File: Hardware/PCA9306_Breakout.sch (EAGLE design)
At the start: 15 parts

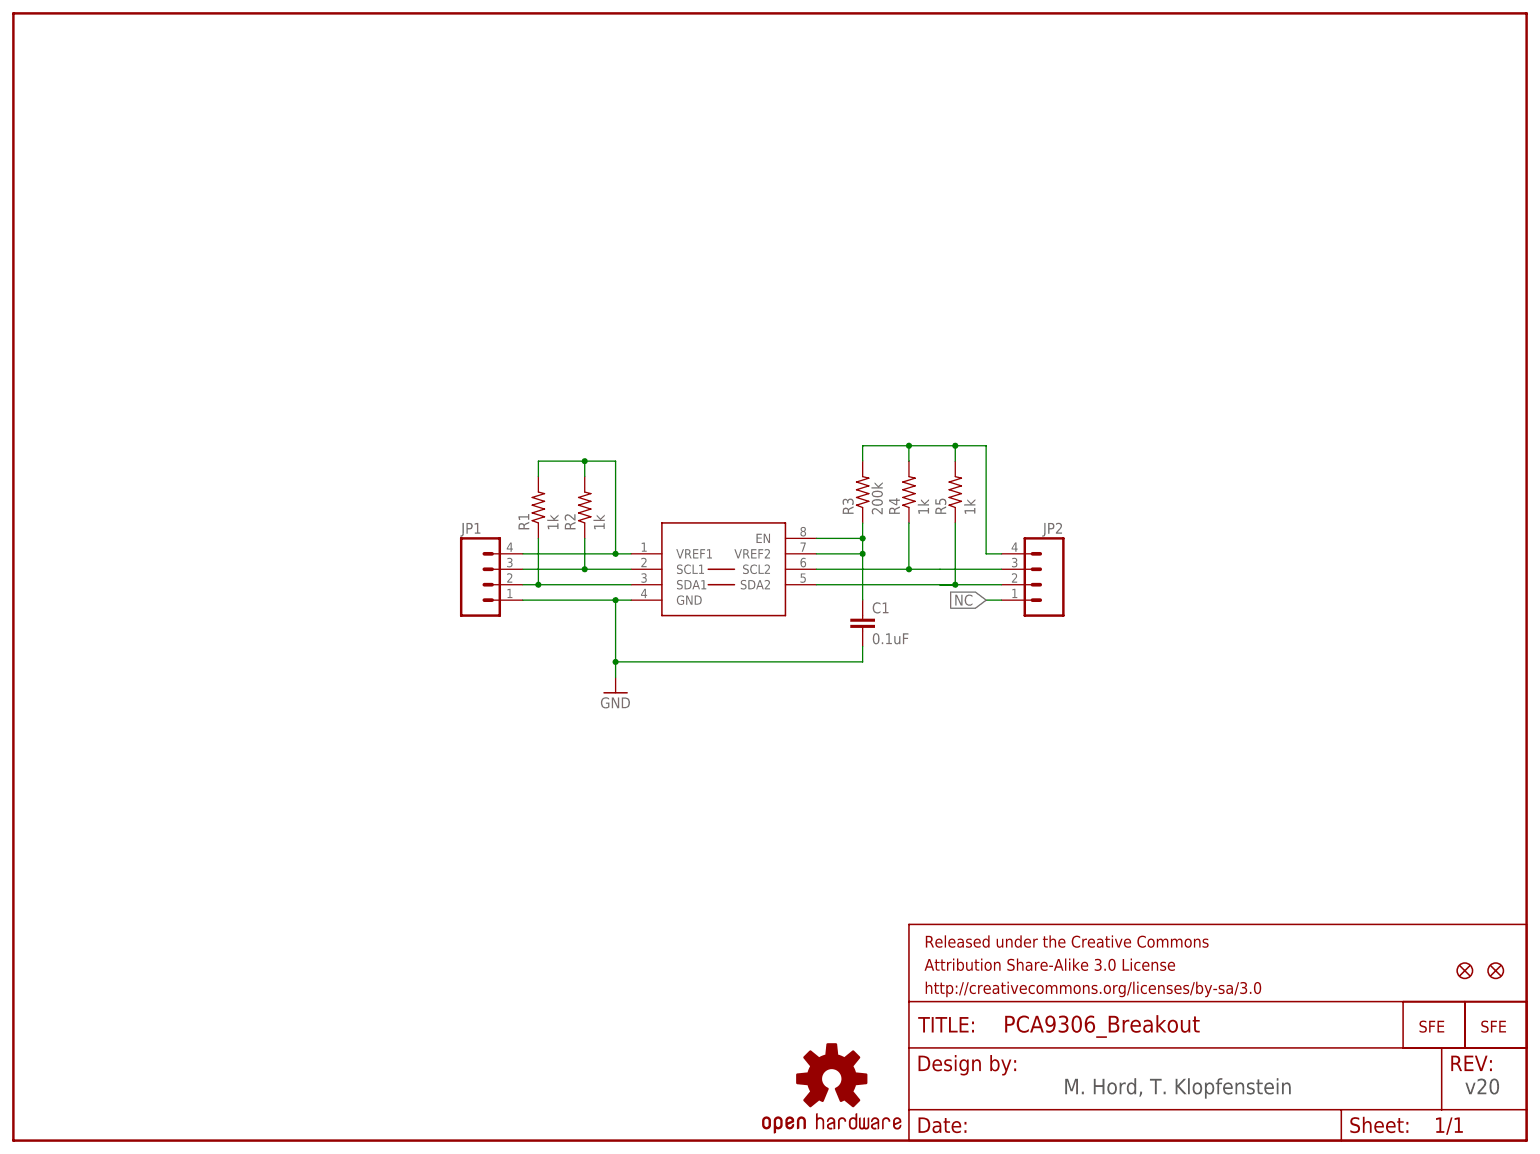
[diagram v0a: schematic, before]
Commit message: Rerouted traces away from IC and changed packages to 0603. Add labels to the schematic on the header pins.
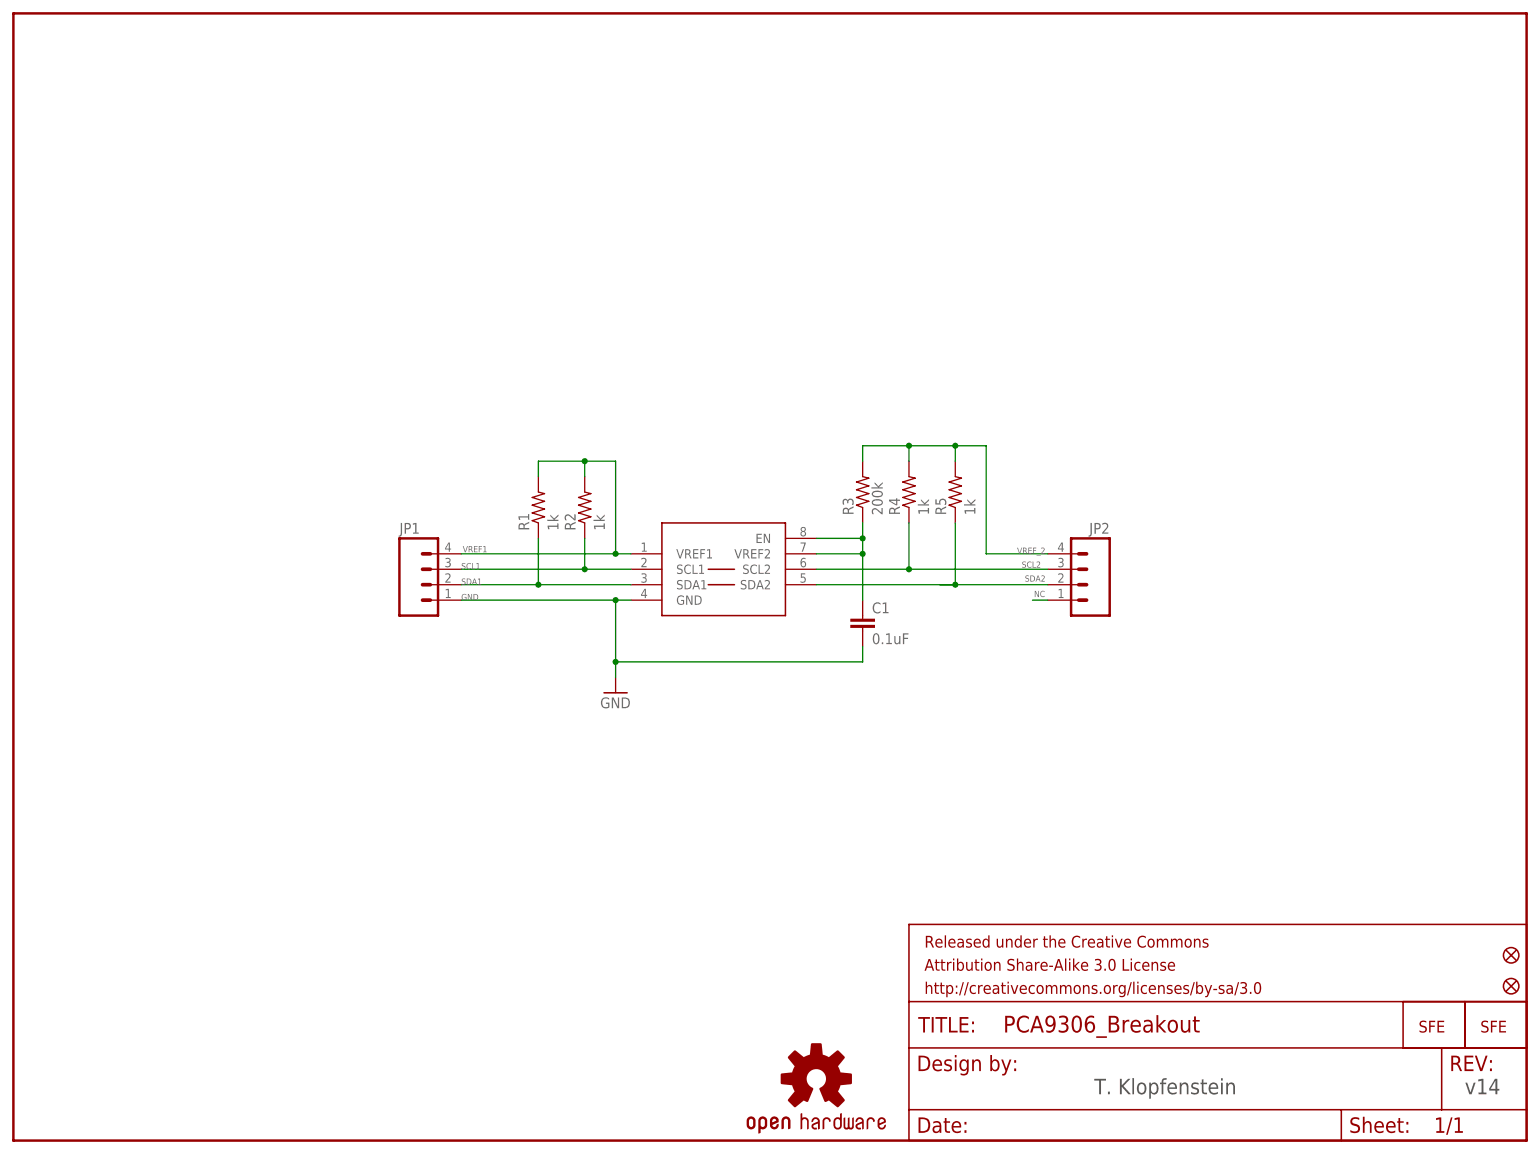
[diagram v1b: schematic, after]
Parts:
- C1: device SparkFun:CAP0402-CAP -> SparkFun:CAP0603-CAP
- R1, R2, R3, R4, R5: device SparkFun:RESISTOR0402-RES -> SparkFun:RESISTOR0603-RES
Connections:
- new net VREF_2: JP2.4, R3.2, R4.2, R5.2
- net VREF2: no longer JP2.4, R3.2, R4.2, R5.2
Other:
- note added: "T. Klopfenstein"
- note added: "v14"
- note removed: "M. Hord, T. Klopfenstein"
- note removed: "v20"
- moved on the sheet: JP1, JP2
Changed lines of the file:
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@@
 <part name="FRAME1" library="SparkFun-Aesthetics" deviceset="FRAME-LETTER" device=""/>
 <part name="U$1" library="miscellany" deviceset="PCA9306" device=""/>
-<part name="R1" library="SparkFun" deviceset="RESISTOR" device="0402-RES" value="1k"/>
-<part name="R2" library="SparkFun" deviceset="RESISTOR" device="0402-RES" value="1k"/>
-<part name="R3" library="SparkFun" deviceset="RESISTOR" device="0402-RES" value="200k"/>
-<part name="R4" library="SparkFun" deviceset="RESISTOR" device="0402-RES" value="1k"/>
-<part name="R5" library="SparkFun" deviceset="RESISTOR" device="0402-RES" value="1k"/>
-<part name="C1" library="SparkFun" deviceset="CAP" device="0402-CAP" value="0.1uF"/>
+<part name="R1" library="SparkFun" deviceset="RESISTOR" device="0603-RES" value="1k"/>
+<part name="R2" library="SparkFun" deviceset="RESISTOR" device="0603-RES" value="1k"/>
+<part name="R3" library="SparkFun" deviceset="RESISTOR" device="0603-RES" value="200k"/>
+<part name="R4" library="SparkFun" deviceset="RESISTOR" device="0603-RES" value="1k"/>
+<part name="R5" library="SparkFun" deviceset="RESISTOR" device="0603-RES" value="1k"/>
+<part name="C1" library="SparkFun" deviceset="CAP" device="0603-CAP" value="0.1uF"/>
 <part name="GND1" library="SparkFun" deviceset="GND" device=""/>
 <part name="JP1" library="SparkFun" deviceset="M04" device="PTH"/>
@@
 <sheet>
 <plain>
-<text x="172.72" y="7.62" size="2.54" layer="97">M. Hord, T. Klopfenstein</text>
-<text x="238.76" y="7.62" size="2.54" layer="97">v20</text>
+<text x="177.8" y="7.62" size="2.54" layer="97">T. Klopfenstein</text>
+<text x="238.76" y="7.62" size="2.54" layer="97">v14</text>
 </plain>
 <instances>
@@
 <instance part="C1" gate="G$1" x="139.7" y="83.82"/>
 <instance part="GND1" gate="1" x="99.06" y="73.66"/>
-<instance part="JP1" gate="G$1" x="78.74" y="91.44"/>
-<instance part="JP2" gate="G$1" x="167.64" y="91.44" rot="MR0"/>
+<instance part="JP1" gate="G$1" x="68.58" y="91.44"/>
+<instance part="JP2" gate="G$1" x="175.26" y="91.44" rot="MR0"/>
 <instance part="JP3" gate="G$1" x="241.3" y="17.78"/>
 <instance part="JP4" gate="G$1" x="231.14" y="17.78"/>
-<instance part="JP7" gate="G$1" x="238.76" y="27.94"/>
-<instance part="JP8" gate="G$1" x="243.84" y="27.94"/>
-<instance part="LOGO1" gate="G$1" x="134.62" y="10.16"/>
+<instance part="JP7" gate="G$1" x="246.38" y="30.48"/>
+<instance part="JP8" gate="G$1" x="246.38" y="25.4"/>
+<instance part="LOGO1" gate="G$1" x="132.08" y="10.16"/>
 </instances>
 <busses>
@@
 <wire x1="86.36" y1="111.76" x2="86.36" y2="109.22" width="0.1524" layer="91"/>
 <wire x1="93.98" y1="109.22" x2="93.98" y2="111.76" width="0.1524" layer="91"/>
-<wire x1="99.06" y1="96.52" x2="83.82" y2="96.52" width="0.1524" layer="91"/>
+<wire x1="99.06" y1="96.52" x2="73.66" y2="96.52" width="0.1524" layer="91"/>
 <junction x="93.98" y="111.76"/>
 <junction x="99.06" y="96.52"/>
@@
 <pinref part="R2" gate="G$1" pin="2"/>
 <pinref part="JP1" gate="G$1" pin="4"/>
+<label x="73.914" y="96.774" size="1.016" layer="95"/>
 </segment>
 </net>
@@
 <wire x1="101.6" y1="93.98" x2="93.98" y2="93.98" width="0.1524" layer="91"/>
 <wire x1="93.98" y1="93.98" x2="93.98" y2="99.06" width="0.1524" layer="91"/>
-<wire x1="93.98" y1="93.98" x2="86.36" y2="93.98" width="0.1524" layer="91"/>
-<wire x1="86.36" y1="93.98" x2="83.82" y2="93.98" width="0.1524" layer="91"/>
+<wire x1="93.98" y1="93.98" x2="73.66" y2="93.98" width="0.1524" layer="91"/>
 <junction x="93.98" y="93.98"/>
 <pinref part="U$1" gate="G$1" pin="SCL1"/>
 <pinref part="R2" gate="G$1" pin="1"/>
 <pinref part="JP1" gate="G$1" pin="3"/>
+<label x="73.66" y="93.98" size="1.016" layer="95"/>
 </segment>
 </net>
@@
 <wire x1="101.6" y1="91.44" x2="86.36" y2="91.44" width="0.1524" layer="91"/>
 <wire x1="86.36" y1="91.44" x2="86.36" y2="99.06" width="0.1524" layer="91"/>
-<wire x1="86.36" y1="91.44" x2="83.82" y2="91.44" width="0.1524" layer="91"/>
+<wire x1="86.36" y1="91.44" x2="73.66" y2="91.44" width="0.1524" layer="91"/>
 <junction x="86.36" y="91.44"/>
 <pinref part="U$1" gate="G$1" pin="SDA1"/>
 <pinref part="R1" gate="G$1" pin="1"/>
 <pinref part="JP1" gate="G$1" pin="2"/>
+<label x="73.66" y="91.44" size="1.016" layer="95"/>
 </segment>
 </net>
@@
 <wire x1="139.7" y1="81.28" x2="139.7" y2="78.74" width="0.1524" layer="91"/>
 <wire x1="139.7" y1="78.74" x2="99.06" y2="78.74" width="0.1524" layer="91"/>
-<wire x1="99.06" y1="88.9" x2="83.82" y2="88.9" width="0.1524" layer="91"/>
+<wire x1="99.06" y1="88.9" x2="73.66" y2="88.9" width="0.1524" layer="91"/>
 <junction x="99.06" y="78.74"/>
 <junction x="99.06" y="88.9"/>
@@
 <pinref part="C1" gate="G$1" pin="2"/>
 <pinref part="JP1" gate="G$1" pin="1"/>
+<label x="73.66" y="88.9" size="1.016" layer="95"/>
 </segment>
 </net>
 <net name="VREF2" class="0">
 <segment>
-<wire x1="132.08" y1="99.06" x2="139.7" y2="99.06" width="0.1524" layer="91"/>
-<wire x1="139.7" y1="99.06" x2="139.7" y2="101.6" width="0.1524" layer="91"/>
 <wire x1="139.7" y1="88.9" x2="139.7" y2="96.52" width="0.1524" layer="91"/>
 <wire x1="139.7" y1="96.52" x2="139.7" y2="99.06" width="0.1524" layer="91"/>
+<wire x1="139.7" y1="99.06" x2="139.7" y2="101.6" width="0.1524" layer="91"/>
 <wire x1="132.08" y1="96.52" x2="139.7" y2="96.52" width="0.1524" layer="91"/>
-<junction x="139.7" y="99.06"/>
 <junction x="139.7" y="96.52"/>
 <pinref part="U$1" gate="G$1" pin="VREF2"/>
-<pinref part="U$1" gate="G$1" pin="EN"/>
 <pinref part="R3" gate="G$1" pin="1"/>
 <pinref part="C1" gate="G$1" pin="1"/>
+<pinref part="U$1" gate="G$1" pin="EN"/>
+<wire x1="132.08" y1="99.06" x2="139.7" y2="99.06" width="0.1524" layer="91"/>
+<junction x="139.7" y="99.06"/>
 </segment>
+</net>
+<net name="SCL2" class="0">
+<segment>
+<wire x1="132.08" y1="93.98" x2="147.32" y2="93.98" width="0.1524" layer="91"/>
+<wire x1="147.32" y1="93.98" x2="147.32" y2="101.6" width="0.1524" layer="91"/>
+<wire x1="147.32" y1="93.98" x2="170.18" y2="93.98" width="0.1524" layer="91"/>
+<junction x="147.32" y="93.98"/>
+<pinref part="U$1" gate="G$1" pin="SCL2"/>
+<pinref part="R4" gate="G$1" pin="1"/>
+<pinref part="JP2" gate="G$1" pin="3"/>
+<label x="165.862" y="94.234" size="1.016" layer="95"/>
+</segment>
+</net>
+<net name="SDA2" class="0">
+<segment>
+<wire x1="132.08" y1="91.44" x2="154.94" y2="91.44" width="0.1524" layer="91"/>
+<wire x1="154.94" y1="91.44" x2="154.94" y2="101.6" width="0.1524" layer="91"/>
+<wire x1="154.94" y1="91.44" x2="152.4" y2="91.44" width="0.1524" layer="91"/>
+<wire x1="154.94" y1="91.44" x2="170.18" y2="91.44" width="0.1524" layer="91"/>
+<junction x="154.94" y="91.44"/>
+<pinref part="U$1" gate="G$1" pin="SDA2"/>
+<pinref part="R5" gate="G$1" pin="1"/>
+<pinref part="JP2" gate="G$1" pin="2"/>
+<label x="166.37" y="91.948" size="1.016" layer="95"/>
+</segment>
+</net>
+<net name="VREF_2" class="0">
 <segment>
 <wire x1="154.94" y1="114.3" x2="154.94" y2="111.76" width="0.1524" layer="91"/>
@@
 <wire x1="139.7" y1="114.3" x2="147.32" y2="114.3" width="0.1524" layer="91"/>
 <wire x1="139.7" y1="111.76" x2="139.7" y2="114.3" width="0.1524" layer="91"/>
-<wire x1="162.56" y1="96.52" x2="160.02" y2="96.52" width="0.1524" layer="91"/>
+<wire x1="170.18" y1="96.52" x2="160.02" y2="96.52" width="0.1524" layer="91"/>
 <wire x1="160.02" y1="96.52" x2="160.02" y2="114.3" width="0.1524" layer="91"/>
 <wire x1="160.02" y1="114.3" x2="154.94" y2="114.3" width="0.1524" layer="91"/>
@@
 <pinref part="R3" gate="G$1" pin="2"/>
 <pinref part="JP2" gate="G$1" pin="4"/>
-</segment>
-</net>
-<net name="SCL2" class="0">
-<segment>
-<wire x1="132.08" y1="93.98" x2="147.32" y2="93.98" width="0.1524" layer="91"/>
-<wire x1="147.32" y1="93.98" x2="147.32" y2="101.6" width="0.1524" layer="91"/>
-<wire x1="147.32" y1="93.98" x2="152.4" y2="93.98" width="0.1524" layer="91"/>
-<wire x1="152.4" y1="93.98" x2="162.56" y2="93.98" width="0.1524" layer="91"/>
-<junction x="147.32" y="93.98"/>
-<pinref part="U$1" gate="G$1" pin="SCL2"/>
-<pinref part="R4" gate="G$1" pin="1"/>
-<pinref part="JP2" gate="G$1" pin="3"/>
-</segment>
-</net>
-<net name="SDA2" class="0">
-<segment>
-<wire x1="132.08" y1="91.44" x2="154.94" y2="91.44" width="0.1524" layer="91"/>
-<wire x1="154.94" y1="91.44" x2="154.94" y2="101.6" width="0.1524" layer="91"/>
-<wire x1="154.94" y1="91.44" x2="152.4" y2="91.44" width="0.1524" layer="91"/>
-<wire x1="152.4" y1="91.44" x2="162.56" y2="91.44" width="0.1524" layer="91"/>
-<junction x="154.94" y="91.44"/>
-<pinref part="U$1" gate="G$1" pin="SDA2"/>
-<pinref part="R5" gate="G$1" pin="1"/>
-<pinref part="JP2" gate="G$1" pin="2"/>
+<label x="165.1" y="96.52" size="1.016" layer="95"/>
 </segment>
 </net>
@@
 <segment>
 <pinref part="JP2" gate="G$1" pin="1"/>
-<wire x1="162.56" y1="88.9" x2="160.02" y2="88.9" width="0.1524" layer="91"/>
-<label x="160.02" y="88.9" size="1.778" layer="95" rot="R180" xref="yes"/>
+<wire x1="170.18" y1="88.9" x2="167.64" y2="88.9" width="0.1524" layer="91"/>
+<label x="167.894" y="89.408" size="1.016" layer="95"/>
 </segment>
 </net>
